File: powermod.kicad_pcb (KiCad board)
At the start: 4 copper layers, 27 x 18 mm, 21 parts, among them J1 Conn_02x07_Odd_Even, J2 Conn_02x07_Odd_Even, U1 TPS54260DGQ

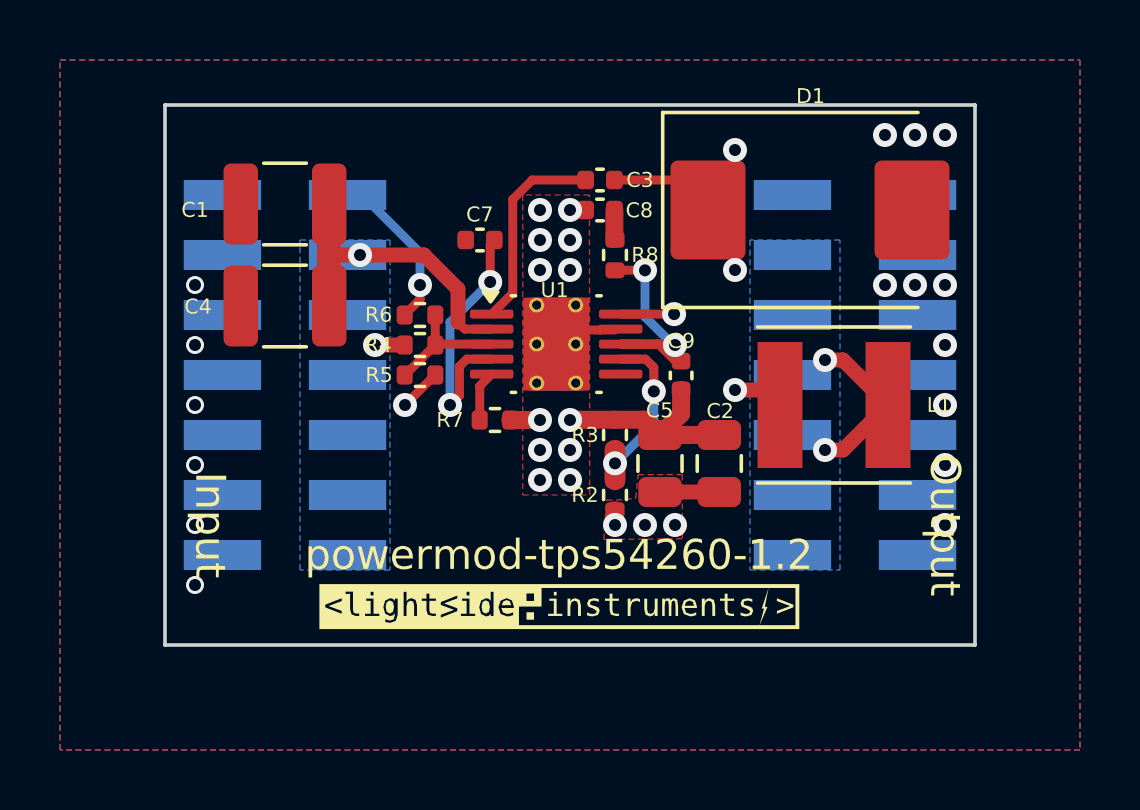
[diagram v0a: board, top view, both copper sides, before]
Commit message: feat: shorter and more shielded signal paths
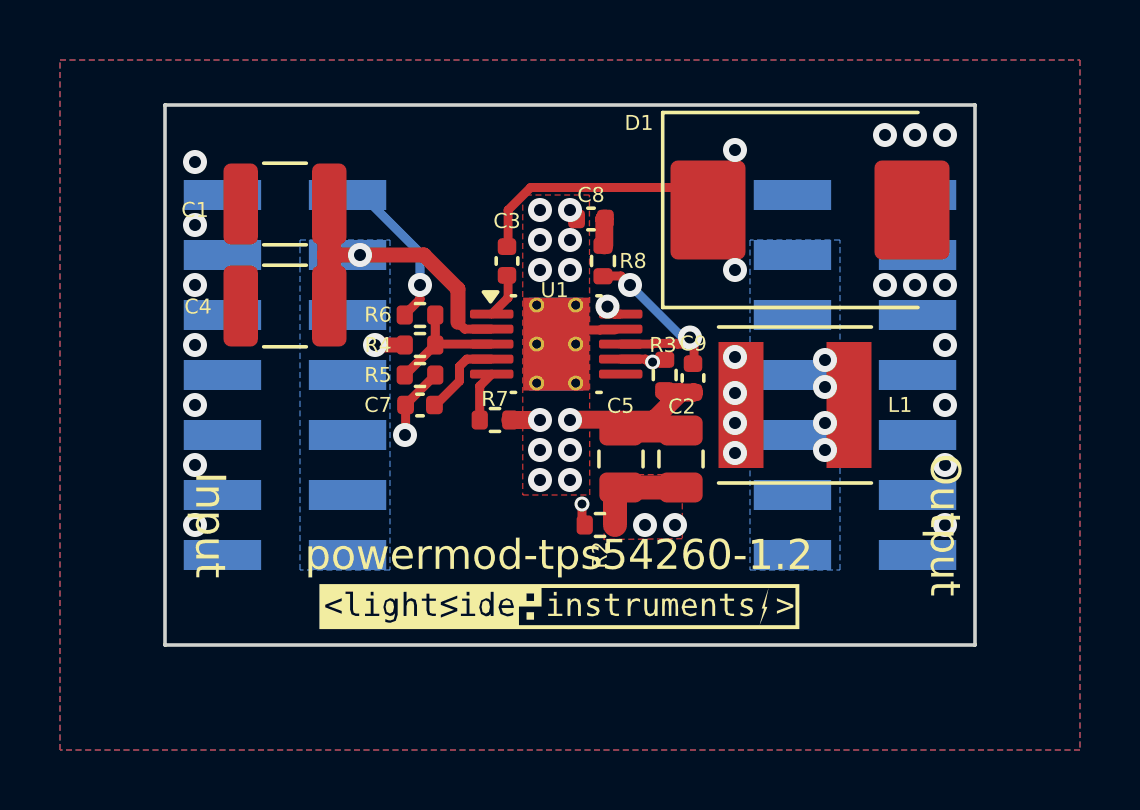
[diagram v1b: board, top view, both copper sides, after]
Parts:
- moved C7 5.85 mm to (24.5, 49.0)
- moved C3 4.11 mm to (27.4, 44.2), turned to -90 degrees
- moved R3 2.60 mm to (32.7, 48.0), turned to -90 degrees
- moved C5 1.31 mm to (31.2, 50.8)
- moved L1 1.30 mm to (37.0, 49.0)
- moved C2 1.29 mm to (33.2, 50.8)
- moved R2 1.12 mm to (30.5, 53.0), turned to 180 degrees
- moved R8 0.45 mm to (30.6, 44.2)
- moved C8 0.42 mm to (30.2, 42.8)
- moved C9 0.40 mm to (33.6, 48.1)
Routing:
- net Net-(U1-SS/TR): track 8.70 -> 2.83 mm, vias 2 -> 0
- net /BOOT: track 6.81 -> 1.49 mm
- net /SW: track 16.1 -> 20.4 mm, vias 4 -> 7
- net +5V: track 7.91 -> 3.56 mm, vias 5 -> 6
- net GND: track 9.40 -> 11.1 mm, vias 29 -> 30
- net /FB: track 6.48 -> 7.54 mm
- net Net-(U1-COMP): track 7.80 -> 7.05 mm

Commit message: feat: shorter paths
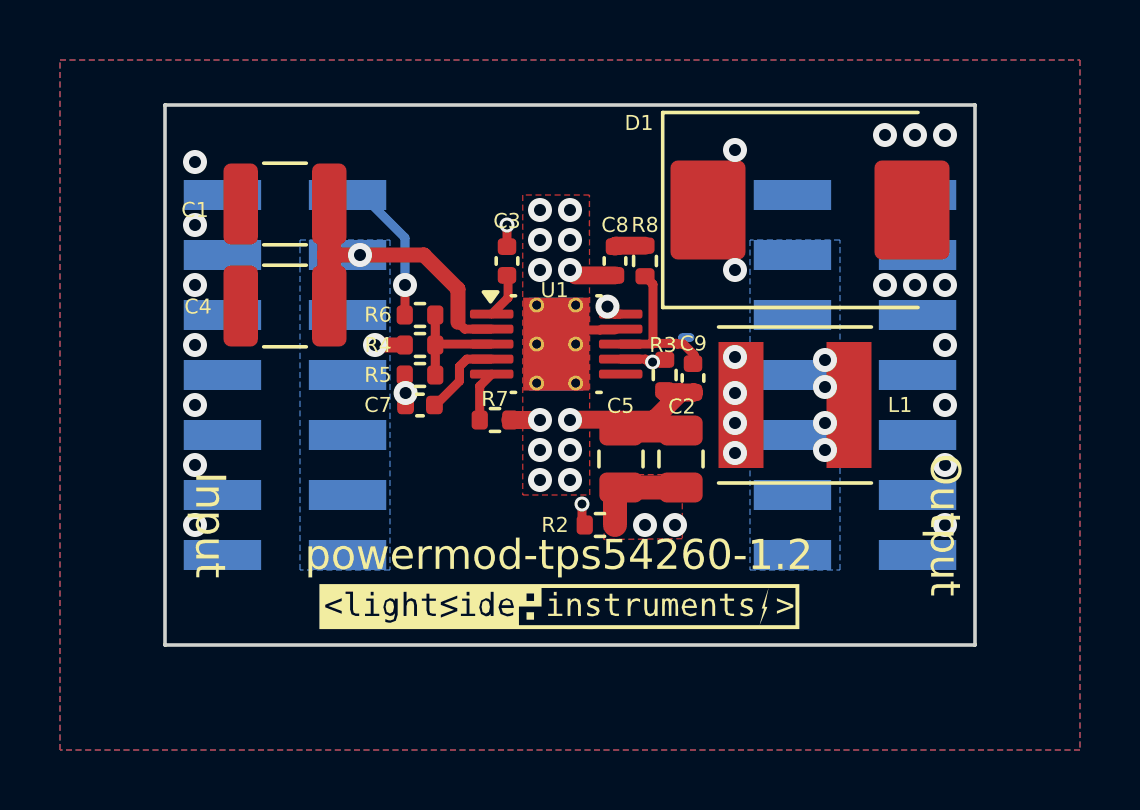
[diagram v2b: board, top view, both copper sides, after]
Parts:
- moved C8 1.61 mm to (31.0, 44.2), turned to 90 degrees
- moved R8 1.40 mm to (32.0, 44.2)
- turned R5 to 0 degrees
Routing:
- net /SW: track 20.4 -> 22.1 mm, vias 7 -> 8
- net Net-(U1-COMP): track 7.05 -> 5.47 mm, vias 2 -> 0
